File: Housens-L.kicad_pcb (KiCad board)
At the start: 2 copper layers, 50 x 50 mm, 33 parts, among them J1 JTAG/SWD, J2 USB_C_2.0, SW1 RESET, U1 MCP1603, U2 BME280, U4 STM32WB55CGUx

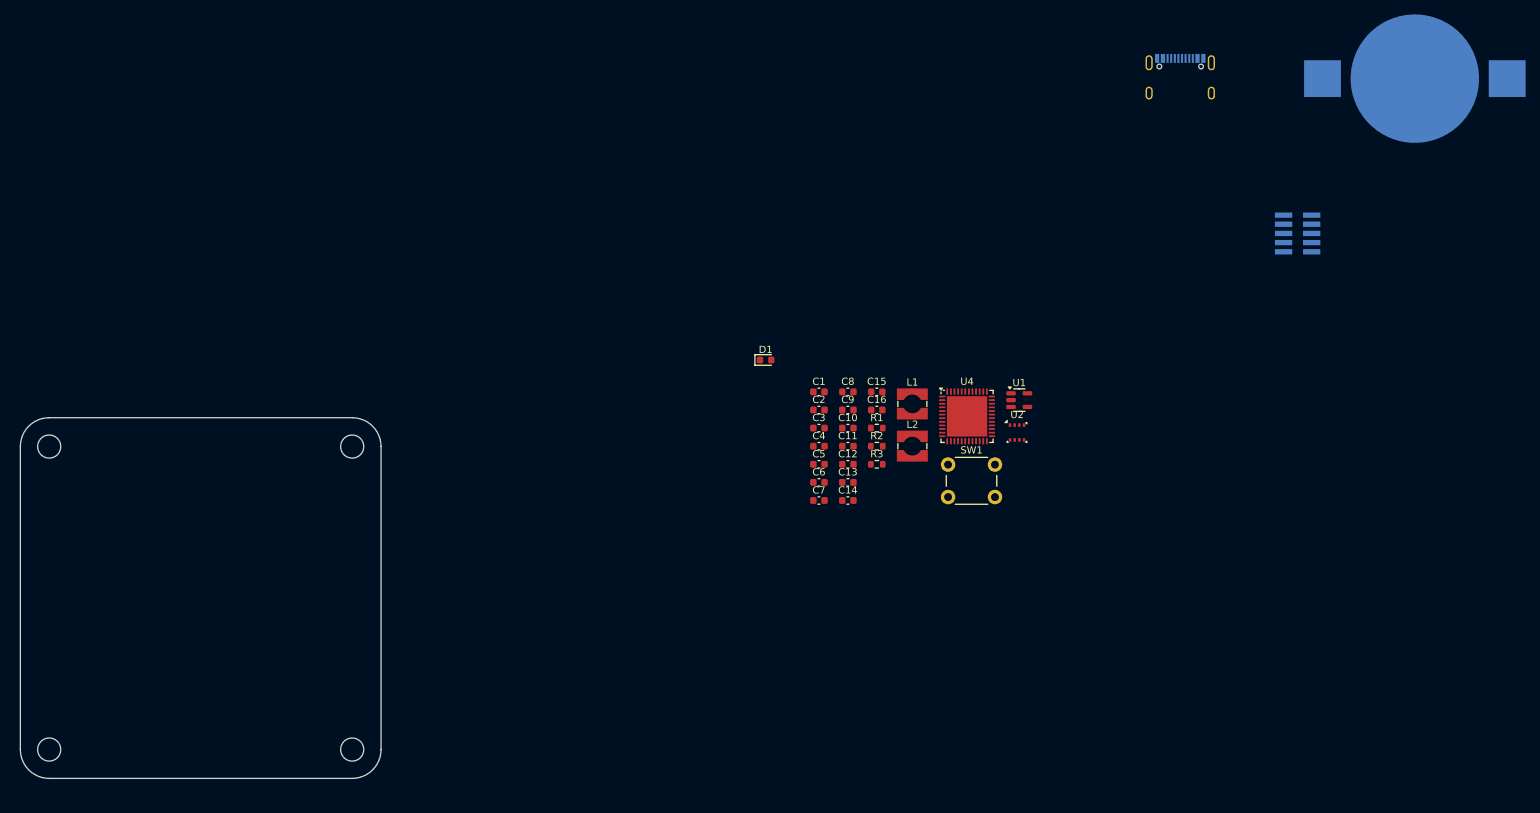
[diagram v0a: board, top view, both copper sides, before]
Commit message: Initial spatial layout
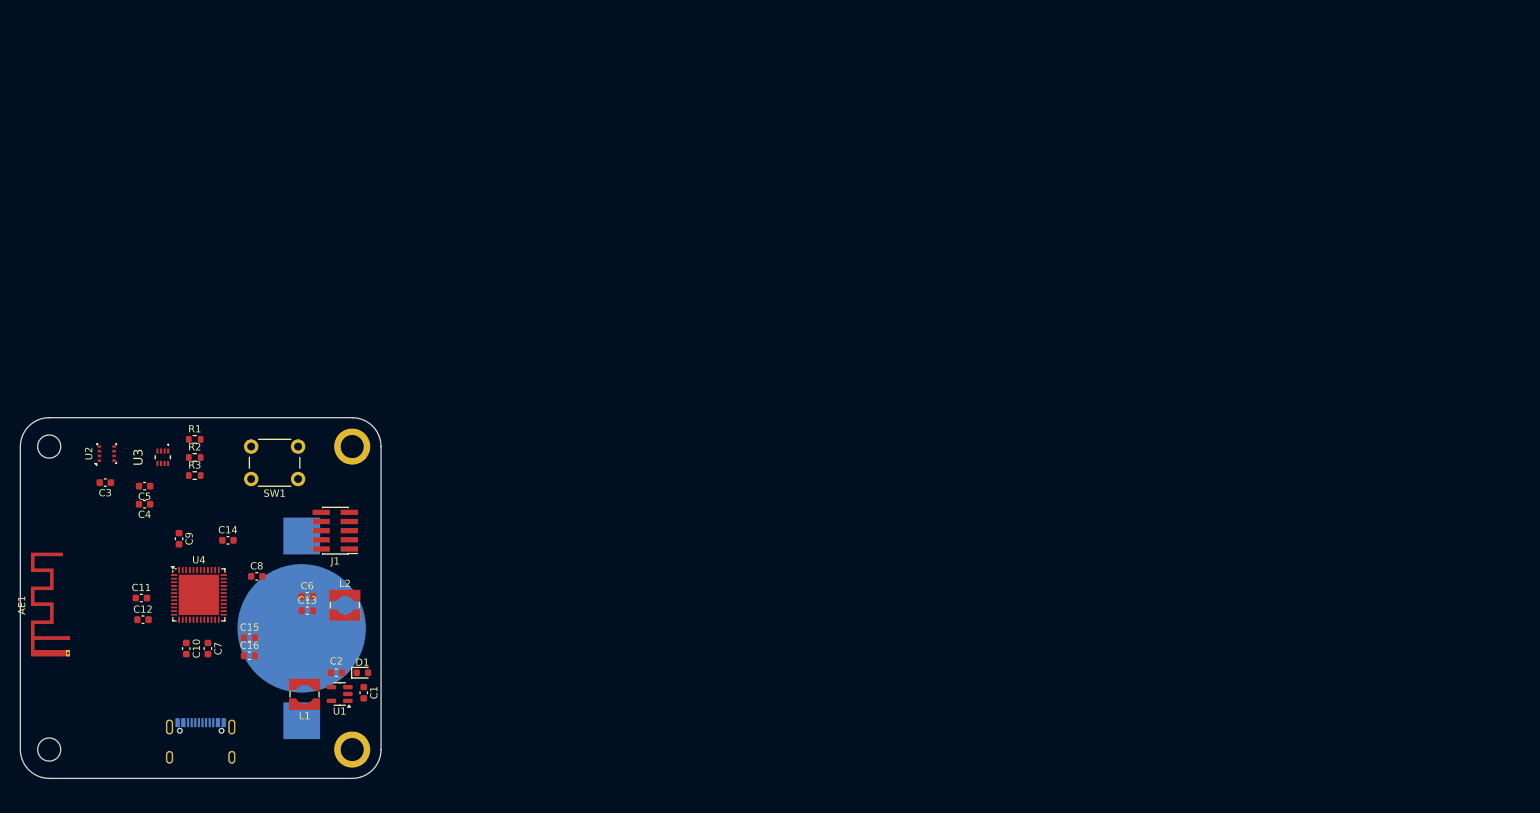
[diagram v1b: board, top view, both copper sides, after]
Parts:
- added AE1: 2.4GHz, RF_Antenna:Texas_SWRA117D_2.4GHz_Right, F.Cu at (66.6, 110.5)
- added U3: OPT3005, Imported:OPT3005DTSR, F.Cu at (79.8, 85.5)
- J1: moved to F.Cu
- moved BT1 172.1 mm to (99.0, 109.2), turned to 90 degrees
- moved J2 164.1 mm to (85.0, 126.0)
- moved J1 139.6 mm to (103.7, 95.7)
- moved U2 126.2 mm to (72.0, 85.0), turned to 90 degrees
- moved U4 109.3 mm to (84.8, 104.6)
- moved U1 102.6 mm to (104.3, 118.3), turned to 180 degrees
- moved C11 100.2 mm to (76.8, 105.0)
- moved C12 100.1 mm to (77.0, 108.0)
- moved C3 99.2 mm to (71.8, 89.0), turned to 180 degrees
- moved C10 96.7 mm to (83.0, 112.0), turned to -90 degrees
- moved R1 94.6 mm to (84.2, 83.0)
- moved R2 94.6 mm to (84.2, 85.5)
- moved R3 94.6 mm to (84.2, 88.0)
- moved C9 94.4 mm to (82.0, 96.8), turned to -90 degrees
- moved C4 93.8 mm to (77.2, 92.0), turned to 180 degrees
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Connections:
- H2 pad : (no net) -> GND
- H3 pad : (no net) -> GND
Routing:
- added copper zone on In1.Cu, net GND
- added copper zone on In2.Cu, net GND
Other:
- copper layers 2 -> 4

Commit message: Graphics
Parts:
- H2, H3: value MountingHole_M3 -> MountingHole_Pad; footprint MountingHole:MountingHole_3.2mm_M3 -> MountingHole:MountingHole_3.2mm_M3_DIN965_Pad
- moved D1 4.86 mm to (107.5, 120.2), turned to -90 degrees
- moved C1 1.63 mm to (107.5, 116.5), turned to 90 degrees
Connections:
- BT1 pad 1: Net-(BT1-+) -> /CELL
- D1 pad 2: Net-(BT1-+) -> /CELL
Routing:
- net /CELL: track 0.00 -> 5.62 mm
- added copper zone on F.Cu, net +BATT
- added copper zone on B.Cu, net /CELL
- added copper zone on B.Cu, net GND
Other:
- board text added: "${CURRENT_DATE}"
- board text added: "BLE Y Thread"
- board text added: "HPT-L"
- board text added: "Housens"
- board text added: "I"

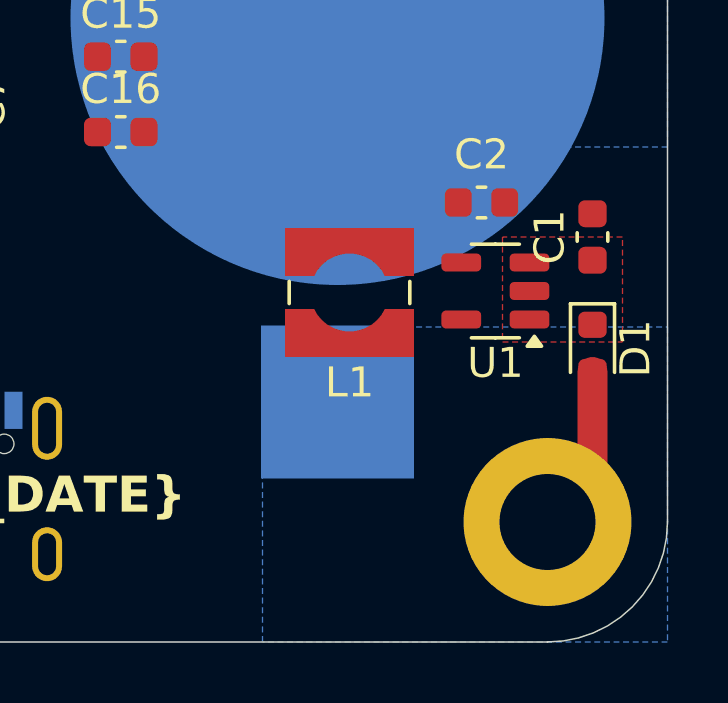
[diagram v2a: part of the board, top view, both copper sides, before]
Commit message: Layout power supply
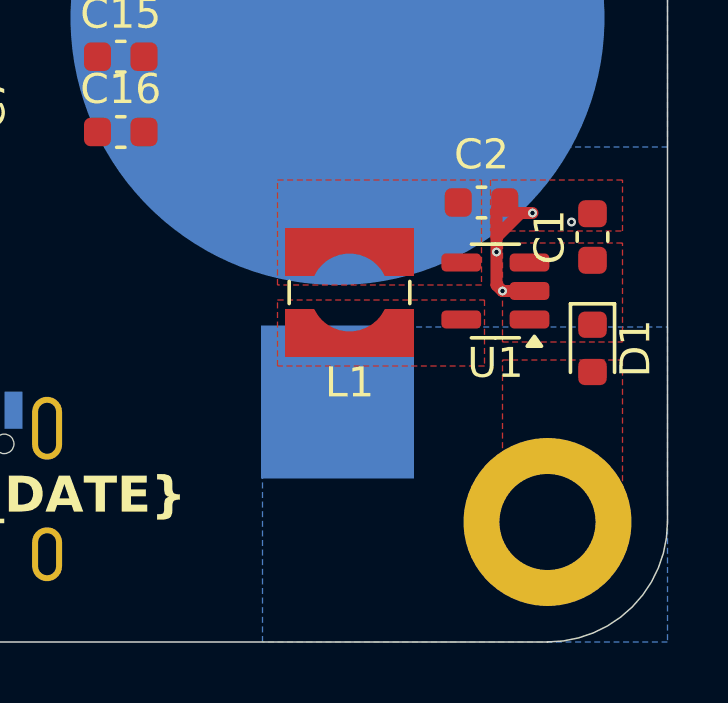
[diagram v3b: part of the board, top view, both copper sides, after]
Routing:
- net GND: track 0.00 -> 6.08 mm, vias 0 -> 4
- net /CELL: track 5.62 -> 0.00 mm
- added copper zone on F.Cu, net +1V8
- added copper zone on F.Cu, net /CELL
- added copper zone on F.Cu, net GND
- added copper zone on F.Cu, net Net-(U1-L_{X})
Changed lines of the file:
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@@
 	)
 	(segment
-		(start 107.5 124.5)
-		(end 106 126)
-		(width 1)
-		(layer "F.Cu")
+		(start 104.3 117)
+		(end 104.3 116.5)
+		(width 0.2)
+		(layer "F.Cu")
+		(net 2)
+	)
+	(segment
+		(start 105.4 118.3)
+		(end 104.5 118.3)
+		(width 0.4)
+		(layer "F.Cu")
+		(net 2)
+	)
+	(segment
+		(start 104.5 118.3)
+		(end 104.3 118.1)
+		(width 0.4)
+		(layer "F.Cu")
+		(net 2)
+	)
+	(segment
+		(start 104.3 118.1)
+		(end 104.3 115.625)
+		(width 0.4)
+		(layer "F.Cu")
+		(net 2)
+	)
+	(segment
+		(start 104.3 116.5)
+		(end 105.1 115.7)
+		(width 0.4)
+		(layer "F.Cu")
+		(net 2)
+	)
+	(segment
+		(start 105.1 115.7)
+		(end 105.5 115.7)
+		(width 0.4)
+		(layer "F.Cu")
+		(net 2)
+	)
+	(segment
+		(start 104.3 115.625)
+		(end 104.575 115.35)
+		(width 0.4)
+		(layer "F.Cu")
+		(net 2)
+	)
+	(via micro
+		(at 106.8 116)
+		(size 0.3)
+		(drill 0.15)
+		(layers "F.Cu" "B.Cu")
+		(remove_unused_layers yes)
+		(keep_end_layers no)
+		(zone_layer_connections "F.Cu" "In1.Cu" "In2.Cu")
+		(net 2)
+	)
+	(via micro
+		(at 105.5 115.7)
+		(size 0.3)
+		(drill 0.15)
+		(layers "F.Cu" "B.Cu")
+		(remove_unused_layers yes)
+		(keep_end_layers no)
+		(zone_layer_connections "F.Cu" "In1.Cu" "In2.Cu")
+		(net 2)
+	)
+	(via micro
+		(at 104.5 118.3)
+		(size 0.3)
+		(drill 0.15)
+		(layers "F.Cu" "B.Cu")
+		(remove_unused_layers yes)
+		(keep_end_layers no)
+		(zone_layer_connections "In1.Cu" "In2.Cu")
+		(net 2)
+	)
+	(via micro
+		(at 104.3 117)
+		(size 0.3)
+		(drill 0.15)
+		(layers "F.Cu" "B.Cu")
+		(remove_unused_layers yes)
+		(keep_end_layers no)
+		(zone_layer_connections "In1.Cu" "In2.Cu")
+		(net 2)
+	)
+	(zone
 		(net 35)
-	)
-	(segment
-		(start 107.5 121)
-		(end 107.5 124.5)
-		(width 1)
-		(layer "F.Cu")
-		(net 35)
+		(net_name "/CELL")
+		(layer "F.Cu")
+		(hatch edge 0.5)
+		(priority 8)
+		(connect_pads thru_hole_only
+			(clearance 0.25)
+		)
+		(min_thickness 0.5)
+		(filled_areas_thickness no)
+		(fill yes
+			(thermal_gap 0.5)
+			(thermal_bridge_width 0.5)
+			(smoothing chamfer)
+			(radius 0.5)
+		)
+		(polygon
+			(pts
+				(xy 104.5 120.6) (xy 108.5 120.6) (xy 108.5 126.1) (xy 104.5 126.1)
+			)
+		)
 	)
 	(zone
@@
 		(priority 4)
 		(connect_pads thru_hole_only
+			(clearance 0.25)
+		)
+		(min_thickness 0.5)
+		(filled_areas_thickness no)
+		(fill yes
+			(thermal_gap 0.5)
+			(thermal_bridge_width 0.5)
+			(smoothing chamfer)
+			(radius 0.5)
+		)
+		(polygon
+			(pts
+				(xy 104.5 120) (xy 108.5 120) (xy 108.5 116.7) (xy 104.5 116.7)
+			)
+		)
+	)
+	(zone
+		(net 5)
+		(net_name "Net-(U1-L_{X})")
+		(layer "F.Cu")
+		(hatch edge 0.5)
+		(priority 6)
+		(connect_pads thru_hole_only
 			(clearance 0)
 		)
@@
 		(polygon
 			(pts
-				(xy 104.5 120) (xy 108.5 120) (xy 108.5 116.5) (xy 104.5 116.5)
-			)
-		)
+				(xy 97 118.6) (xy 103.9 118.6) (xy 103.9 120.8) (xy 97 120.8)
+			)
+		)
+	)
+	(zone
+		(net 3)
+		(net_name "+1V8")
+		(layer "F.Cu")
+		(hatch edge 0.5)
+		(priority 5)
+		(connect_pads thru_hole_only
+			(clearance 0)
+		)
+		(min_thickness 0.25)
+		(filled_areas_thickness no)
+		(fill yes
+			(thermal_gap 0.5)
+			(thermal_bridge_width 0.5)
+			(smoothing chamfer)
+			(radius 0.5)
+		)
+		(polygon
+			(pts
+				(xy 103.8 114.6) (xy 103.8 118.1) (xy 97 118.1) (xy 97 114.6)
+			)
+		)
+	)
+	(zone
+		(net 2)
+		(net_name "GND")
+		(layer "F.Cu")
+		(hatch edge 0.5)
+		(priority 7)
+		(connect_pads thru_hole_only
+			(clearance 0)
+		)
+		(min_thickness 0.25)
+		(filled_areas_thickness no)
+		(fill yes
+			(thermal_gap 0.5)
+			(thermal_bridge_width 0.5)
+			(smoothing chamfer)
+			(radius 0.5)
+		)
+		(polygon
+			(pts
+				(xy 108.5 116.3) (xy 108.5 114.6) (xy 104.1 114.6) (xy 104.1 116.3)
+			)
+		)

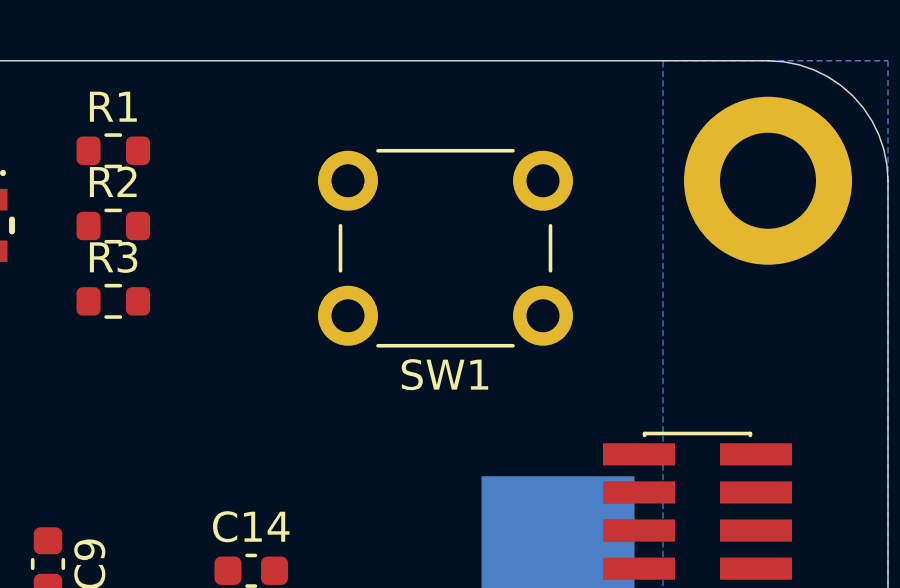
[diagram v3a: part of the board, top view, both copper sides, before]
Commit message: Add TODO about touchsense
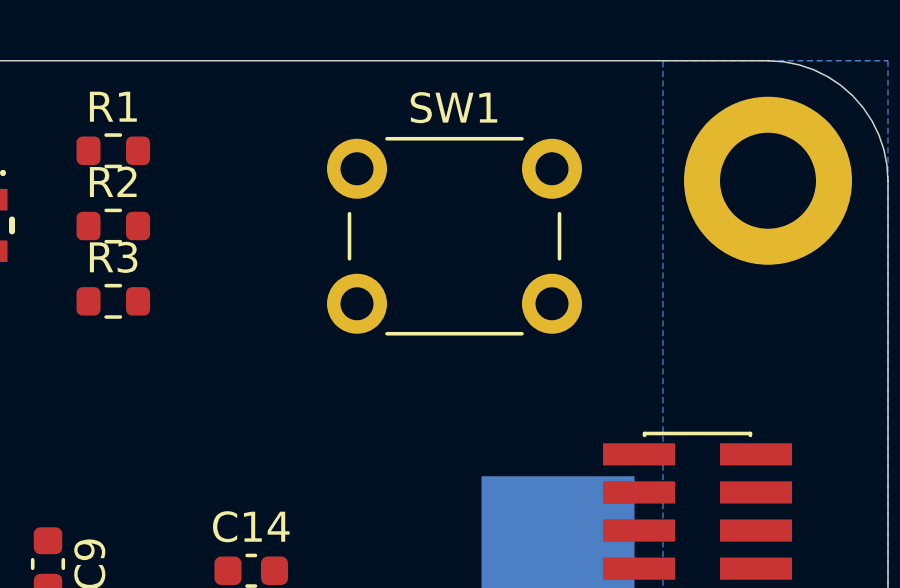
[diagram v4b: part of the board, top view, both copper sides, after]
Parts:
- moved SW1 7.90 mm to (92.3, 83.6), turned to 0 degrees
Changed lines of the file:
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@@
 	(footprint "Button_Switch_THT:SW_PUSH_6mm"
 		(layer "F.Cu")
-		(at 98.5 88.5 180)
+		(at 92.3 83.6)
 		(descr "Generic 6mm SW tactile push button")
 		(tags "tact sw push 6mm")
@@
 		)
 		(property "Footprint" "Button_Switch_THT:SW_PUSH_6mm"
-			(at 0 0 180)
+			(at 0 0 0)
 			(unlocked yes)
 			(layer "F.Fab")
@@
 		)
 		(property "Datasheet" ""
-			(at 0 0 180)
+			(at 0 0 0)
 			(unlocked yes)
 			(layer "F.Fab")
@@
 		)
 		(property "Description" "Push button switch, generic, two pins"
-			(at 0 0 180)
+			(at 0 0 0)
 			(unlocked yes)
 			(layer "F.Fab")
@@
 		(attr through_hole)
 		(fp_line
+			(start -0.25 1.5)
+			(end -0.25 3)
+			(stroke
+				(width 0.12)
+				(type solid)
+			)
+			(layer "F.SilkS")
+		)
+		(fp_line
+			(start 1 5.5)
+			(end 5.5 5.5)
+			(stroke
+				(width 0.12)
+				(type solid)
+			)
+			(layer "F.SilkS")
+		)
+		(fp_line
+			(start 5.5 -1)
+			(end 1 -1)
+			(stroke
+				(width 0.12)
+				(type solid)
+			)
+			(layer "F.SilkS")
+		)
+		(fp_line
 			(start 6.75 3)
 			(end 6.75 1.5)
@@
 		)
 		(fp_line
-			(start 5.5 -1)
-			(end 1 -1)
-			(stroke
-				(width 0.12)
-				(type solid)
-			)
-			(layer "F.SilkS")
-		)
-		(fp_line
-			(start 1 5.5)
-			(end 5.5 5.5)
-			(stroke
-				(width 0.12)
-				(type solid)
-			)
-			(layer "F.SilkS")
-		)
-		(fp_line
-			(start -0.25 1.5)
-			(end -0.25 3)
-			(stroke
-				(width 0.12)
-				(type solid)
-			)
-			(layer "F.SilkS")
+			(start -1.5 -1.5)
+			(end -1.25 -1.5)
+			(stroke
+				(width 0.05)
+				(type solid)
+			)
+			(layer "F.CrtYd")
+		)
+		(fp_line
+			(start -1.5 -1.25)
+			(end -1.5 -1.5)
+			(stroke
+				(width 0.05)
+				(type solid)
+			)
+			(layer "F.CrtYd")
+		)
+		(fp_line
+			(start -1.5 5.75)
+			(end -1.5 -1.25)
+			(stroke
+				(width 0.05)
+				(type solid)
+			)
+			(layer "F.CrtYd")
+		)
+		(fp_line
+			(start -1.5 5.75)
+			(end -1.5 6)
+			(stroke
+				(width 0.05)
+				(type solid)
+			)
+			(layer "F.CrtYd")
+		)
+		(fp_line
+			(start -1.5 6)
+			(end -1.25 6)
+			(stroke
+				(width 0.05)
+				(type solid)
+			)
+			(layer "F.CrtYd")
+		)
+		(fp_line
+			(start -1.25 -1.5)
+			(end 7.75 -1.5)
+			(stroke
+				(width 0.05)
+				(type solid)
+			)
+			(layer "F.CrtYd")
+		)
+		(fp_line
+			(start 7.75 -1.5)
+			(end 8 -1.5)
+			(stroke
+				(width 0.05)
+				(type solid)
+			)
+			(layer "F.CrtYd")
+		)
+		(fp_line
+			(start 7.75 6)
+			(end -1.25 6)
+			(stroke
+				(width 0.05)
+				(type solid)
+			)
+			(layer "F.CrtYd")
+		)
+		(fp_line
+			(start 7.75 6)
+			(end 8 6)
+			(stroke
+				(width 0.05)
+				(type solid)
+			)
+			(layer "F.CrtYd")
+		)
+		(fp_line
+			(start 8 -1.5)
+			(end 8 -1.25)
+			(stroke
+				(width 0.05)
+				(type solid)
+			)
+			(layer "F.CrtYd")
+		)
+		(fp_line
+			(start 8 -1.25)
+			(end 8 5.75)
+			(stroke
+				(width 0.05)
+				(type solid)
+			)
+			(layer "F.CrtYd")
 		)
 		(fp_line
@@
 		)
 		(fp_line
-			(start 8 -1.25)
-			(end 8 5.75)
-			(stroke
-				(width 0.05)
-				(type solid)
-			)
-			(layer "F.CrtYd")
-		)
-		(fp_line
-			(start 8 -1.5)
-			(end 8 -1.25)
-			(stroke
-				(width 0.05)
-				(type solid)
-			)
-			(layer "F.CrtYd")
-		)
-		(fp_line
-			(start 7.75 6)
-			(end 8 6)
-			(stroke
-				(width 0.05)
-				(type solid)
-			)
-			(layer "F.CrtYd")
-		)
-		(fp_line
-			(start 7.75 6)
-			(end -1.25 6)
-			(stroke
-				(width 0.05)
-				(type solid)
-			)
-			(layer "F.CrtYd")
-		)
-		(fp_line
-			(start 7.75 -1.5)
-			(end 8 -1.5)
-			(stroke
-				(width 0.05)
-				(type solid)
-			)
-			(layer "F.CrtYd")
-		)
-		(fp_line
-			(start -1.25 -1.5)
-			(end 7.75 -1.5)
-			(stroke
-				(width 0.05)
-				(type solid)
-			)
-			(layer "F.CrtYd")
-		)
-		(fp_line
-			(start -1.5 6)
-			(end -1.25 6)
-			(stroke
-				(width 0.05)
-				(type solid)
-			)
-			(layer "F.CrtYd")
-		)
-		(fp_line
-			(start -1.5 5.75)
-			(end -1.5 6)
-			(stroke
-				(width 0.05)
-				(type solid)
-			)
-			(layer "F.CrtYd")
-		)
-		(fp_line
-			(start -1.5 5.75)
-			(end -1.5 -1.25)
-			(stroke
-				(width 0.05)
-				(type solid)
-			)
-			(layer "F.CrtYd")
-		)
-		(fp_line
-			(start -1.5 -1.25)
-			(end -1.5 -1.5)
-			(stroke
-				(width 0.05)
-				(type solid)
-			)
-			(layer "F.CrtYd")
-		)
-		(fp_line
-			(start -1.5 -1.5)
-			(end -1.25 -1.5)
-			(stroke
-				(width 0.05)
-				(type solid)
-			)
-			(layer "F.CrtYd")
+			(start 0.25 -0.75)
+			(end 3.25 -0.75)
+			(stroke
+				(width 0.1)
+				(type solid)
+			)
+			(layer "F.Fab")
+		)
+		(fp_line
+			(start 0.25 5.25)
+			(end 0.25 -0.75)
+			(stroke
+				(width 0.1)
+				(type solid)
+			)
+			(layer "F.Fab")
+		)
+		(fp_line
+			(start 3.25 -0.75)
+			(end 6.25 -0.75)
+			(stroke
+				(width 0.1)
+				(type solid)
+			)
+			(layer "F.Fab")
+		)
+		(fp_line
+			(start 6.25 -0.75)
+			(end 6.25 5.25)
+			(stroke
+				(width 0.1)
+				(type solid)
+			)
+			(layer "F.Fab")
 		)
 		(fp_line
 			(start 6.25 5.25)
 			(end 0.25 5.25)
-			(stroke
-				(width 0.1)
-				(type solid)
-			)
-			(layer "F.Fab")
-		)
-		(fp_line
-			(start 6.25 -0.75)
-			(end 6.25 5.25)
-			(stroke
-				(width 0.1)
-				(type solid)
-			)
-			(layer "F.Fab")
-		)
-		(fp_line
-			(start 3.25 -0.75)
-			(end 6.25 -0.75)
-			(stroke
-				(width 0.1)
-				(type solid)
-			)
-			(layer "F.Fab")
-		)
-		(fp_line
-			(start 0.25 5.25)
-			(end 0.25 -0.75)
-			(stroke
-				(width 0.1)
-				(type solid)
-			)
-			(layer "F.Fab")
-		)
-		(fp_line
-			(start 0.25 -0.75)
-			(end 3.25 -0.75)
 			(stroke
 				(width 0.1)
@@
 		)
 		(pad "1" thru_hole circle
-			(at 0 0 270)
+			(at 0 0 90)
 			(size 2 2)
 			(drill 1.1)
@@
 		)
 		(pad "1" thru_hole circle
-			(at 6.5 0 270)
+			(at 6.5 0 90)
 			(size 2 2)
 			(drill 1.1)
@@
 		)
 		(pad "2" thru_hole circle
-			(at 0 4.5 270)
+			(at 0 4.5 90)
 			(size 2 2)
 			(drill 1.1)
@@
 		)
 		(pad "2" thru_hole circle
-			(at 6.5 4.5 270)
+			(at 6.5 4.5 90)
 			(size 2 2)
 			(drill 1.1)
